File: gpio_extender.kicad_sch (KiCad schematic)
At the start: 19 parts, among them SW10 SW_Push, SW3 SW_Push, SW4 SW_Push, SW5 SW_Push, SW6 SW_Push, SW7 SW_Push, SW8 SW_Push, SW9 SW_Push, U6 AW9523B

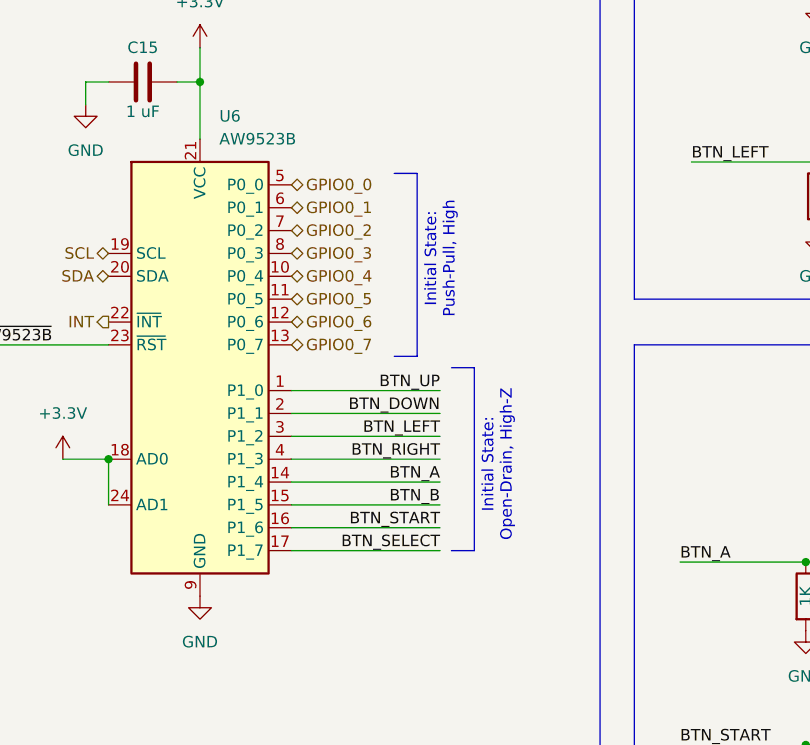
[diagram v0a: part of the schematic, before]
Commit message: Schematics: Add uSD card holder & VBAT sensing
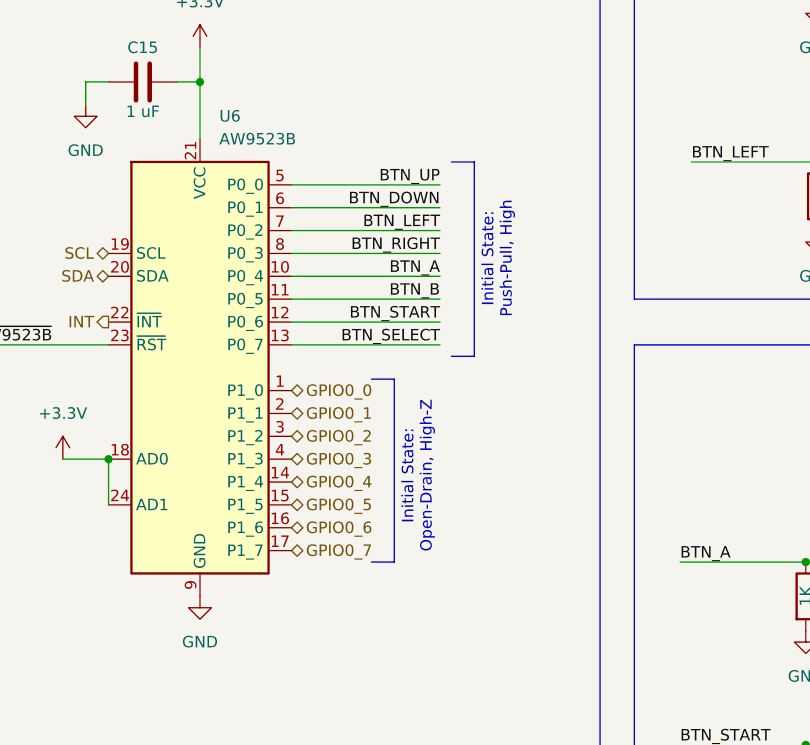
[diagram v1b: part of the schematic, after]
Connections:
- net BTN_A: now also U6.10 (P0_4); no longer U6.14 (P1_4)
- net BTN_B: now also U6.11 (P0_5); no longer U6.15 (P1_5)
- net BTN_DOWN: now also U6.6 (P0_1); no longer U6.2 (P1_1)
- net BTN_LEFT: now also U6.7 (P0_2); no longer U6.3 (P1_2)
- net BTN_RIGHT: now also U6.8 (P0_3); no longer U6.4 (P1_3)
- net BTN_SELECT: now also U6.13 (P0_7); no longer U6.17 (P1_7)
- net BTN_START: now also U6.12 (P0_6); no longer U6.16 (P1_6)
- net BTN_UP: now also U6.5 (P0_0); no longer U6.1 (P1_0)
- net GPIO0_0: now also U6.1 (P1_0); no longer U6.5 (P0_0)
- net GPIO0_1: now also U6.2 (P1_1); no longer U6.6 (P0_1)
- net GPIO0_2: now also U6.3 (P1_2); no longer U6.7 (P0_2)
- net GPIO0_3: now also U6.4 (P1_3); no longer U6.8 (P0_3)
- net GPIO0_4: now also U6.14 (P1_4); no longer U6.10 (P0_4)
- net GPIO0_5: now also U6.15 (P1_5); no longer U6.11 (P0_5)
- net GPIO0_6: now also U6.16 (P1_6); no longer U6.12 (P0_6)
- net GPIO0_7: now also U6.17 (P1_7); no longer U6.13 (P0_7)
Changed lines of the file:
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@@
 	(text "Initial State:\nPush-Pull, High"
 		(exclude_from_sim no)
-		(at 85.09 71.882 90)
+		(at 91.44 71.882 90)
 		(effects
 			(font
@@
 	(text "Initial State:\nOpen-Drain, High-Z"
 		(exclude_from_sim no)
-		(at 91.44 94.742 90)
+		(at 82.55 96.012 90)
 		(effects
 			(font
@@
 	(polyline
 		(pts
-			(xy 88.9 104.14) (xy 88.9 83.82)
+			(xy 80.01 105.41) (xy 80.01 85.09)
 		)
 		(stroke
@@
 	(polyline
 		(pts
-			(xy 82.55 82.55) (xy 82.55 62.23)
+			(xy 88.9 82.55) (xy 88.9 62.23)
 		)
 		(stroke
@@
 	(wire
 		(pts
-			(xy 68.58 86.36) (xy 85.09 86.36)
+			(xy 68.58 63.5) (xy 85.09 63.5)
 		)
 		(stroke
@@
 	(polyline
 		(pts
-			(xy 86.36 104.14) (xy 88.9 104.14)
+			(xy 77.47 105.41) (xy 80.01 105.41)
 		)
 		(stroke
@@
 	(polyline
 		(pts
-			(xy 80.01 62.23) (xy 82.55 62.23)
+			(xy 86.36 60.96) (xy 88.9 60.96)
 		)
 		(stroke
@@
 	(wire
 		(pts
-			(xy 68.58 96.52) (xy 85.09 96.52)
+			(xy 68.58 73.66) (xy 85.09 73.66)
 		)
 		(stroke
@@
 	(wire
 		(pts
-			(xy 68.58 104.14) (xy 85.09 104.14)
+			(xy 68.58 81.28) (xy 85.09 81.28)
 		)
 		(stroke
@@
 	(wire
 		(pts
-			(xy 68.58 93.98) (xy 85.09 93.98)
+			(xy 68.58 71.12) (xy 85.09 71.12)
 		)
 		(stroke
@@
 	(polyline
 		(pts
-			(xy 80.01 82.55) (xy 82.55 82.55)
+			(xy 86.36 82.55) (xy 88.9 82.55)
 		)
 		(stroke
@@
 	(wire
 		(pts
-			(xy 68.58 101.6) (xy 85.09 101.6)
+			(xy 68.58 78.74) (xy 85.09 78.74)
 		)
 		(stroke
@@
 	(polyline
 		(pts
-			(xy 86.36 83.82) (xy 88.9 83.82)
+			(xy 77.47 85.09) (xy 80.01 85.09)
 		)
 		(stroke
@@
 	(wire
 		(pts
-			(xy 68.58 91.44) (xy 85.09 91.44)
+			(xy 68.58 68.58) (xy 85.09 68.58)
 		)
 		(stroke
@@
 	(wire
 		(pts
-			(xy 68.58 88.9) (xy 85.09 88.9)
-		)
-		(stroke
-			(width 0)
-			(type default)
-		)
-	)
-	(wire
-		(pts
-			(xy 68.58 99.06) (xy 85.09 99.06)
+			(xy 68.58 66.04) (xy 85.09 66.04)
+		)
+		(stroke
+			(width 0)
+			(type default)
+		)
+	)
+	(wire
+		(pts
+			(xy 68.58 76.2) (xy 85.09 76.2)
+		)
+		(stroke
+			(width 0)
+			(type default)
+		)
+	)
+	(polyline
+		(pts
+			(xy 88.9 60.96) (xy 88.9 62.23)
 		)
 		(stroke
@@
 	)
 	(label "BTN_DOWN"
-		(at 85.09 88.9 180)
+		(at 85.09 66.04 180)
 		(effects
 			(font
@@
 	)
 	(label "BTN_START"
-		(at 85.09 101.6 180)
+		(at 85.09 78.74 180)
 		(effects
 			(font
@@
 	)
 	(label "BTN_LEFT"
-		(at 85.09 91.44 180)
+		(at 85.09 68.58 180)
 		(effects
 			(font
@@
 	)
 	(label "BTN_UP"
-		(at 85.09 86.36 180)
+		(at 85.09 63.5 180)
 		(effects
 			(font
@@
 	)
 	(label "BTN_A"
-		(at 85.09 96.52 180)
+		(at 85.09 73.66 180)
 		(effects
 			(font
@@
 	)
 	(label "BTN_SELECT"
-		(at 85.09 104.14 180)
+		(at 85.09 81.28 180)
 		(effects
 			(font
@@
 	)
 	(label "BTN_B"
-		(at 85.09 99.06 180)
+		(at 85.09 76.2 180)
 		(effects
 			(font
@@
 	)
 	(label "BTN_RIGHT"
-		(at 85.09 93.98 180)
+		(at 85.09 71.12 180)
 		(effects
 			(font
@@
 	(hierarchical_label "GPIO0_3"
 		(shape bidirectional)
-		(at 68.58 71.12 0)
+		(at 68.58 93.98 0)
 		(effects
 			(font
@@
 	(hierarchical_label "GPIO0_4"
 		(shape bidirectional)
-		(at 68.58 73.66 0)
+		(at 68.58 96.52 0)
 		(effects
 			(font
@@
 	(hierarchical_label "GPIO0_2"
 		(shape bidirectional)
-		(at 68.58 68.58 0)
+		(at 68.58 91.44 0)
 		(effects
 			(font
@@
 	(hierarchical_label "GPIO0_7"
 		(shape bidirectional)
-		(at 68.58 81.28 0)
+		(at 68.58 104.14 0)
 		(effects
 			(font
@@
 	(hierarchical_label "GPIO0_0"
 		(shape bidirectional)
-		(at 68.58 63.5 0)
+		(at 68.58 86.36 0)
 		(effects
 			(font
@@
 	(hierarchical_label "GPIO0_1"
 		(shape bidirectional)
-		(at 68.58 66.04 0)
+		(at 68.58 88.9 0)
 		(effects
 			(font
@@
 	(hierarchical_label "GPIO0_6"
 		(shape bidirectional)
-		(at 68.58 78.74 0)
+		(at 68.58 101.6 0)
 		(effects
 			(font
@@
 	(hierarchical_label "GPIO0_5"
 		(shape bidirectional)
-		(at 68.58 76.2 0)
-		(effects
-			(font
+		(at 68.58 99.06 0)
+		(effects
+			(font
